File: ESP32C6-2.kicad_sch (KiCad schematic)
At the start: 20 parts, among them J1 DE9_Pins, J2 Screw_Terminal_01x04, U1 XIAO-ESP32-C6/SUPERMini, U2 SN65HVD230DR, U3 LMR51430YDDCR

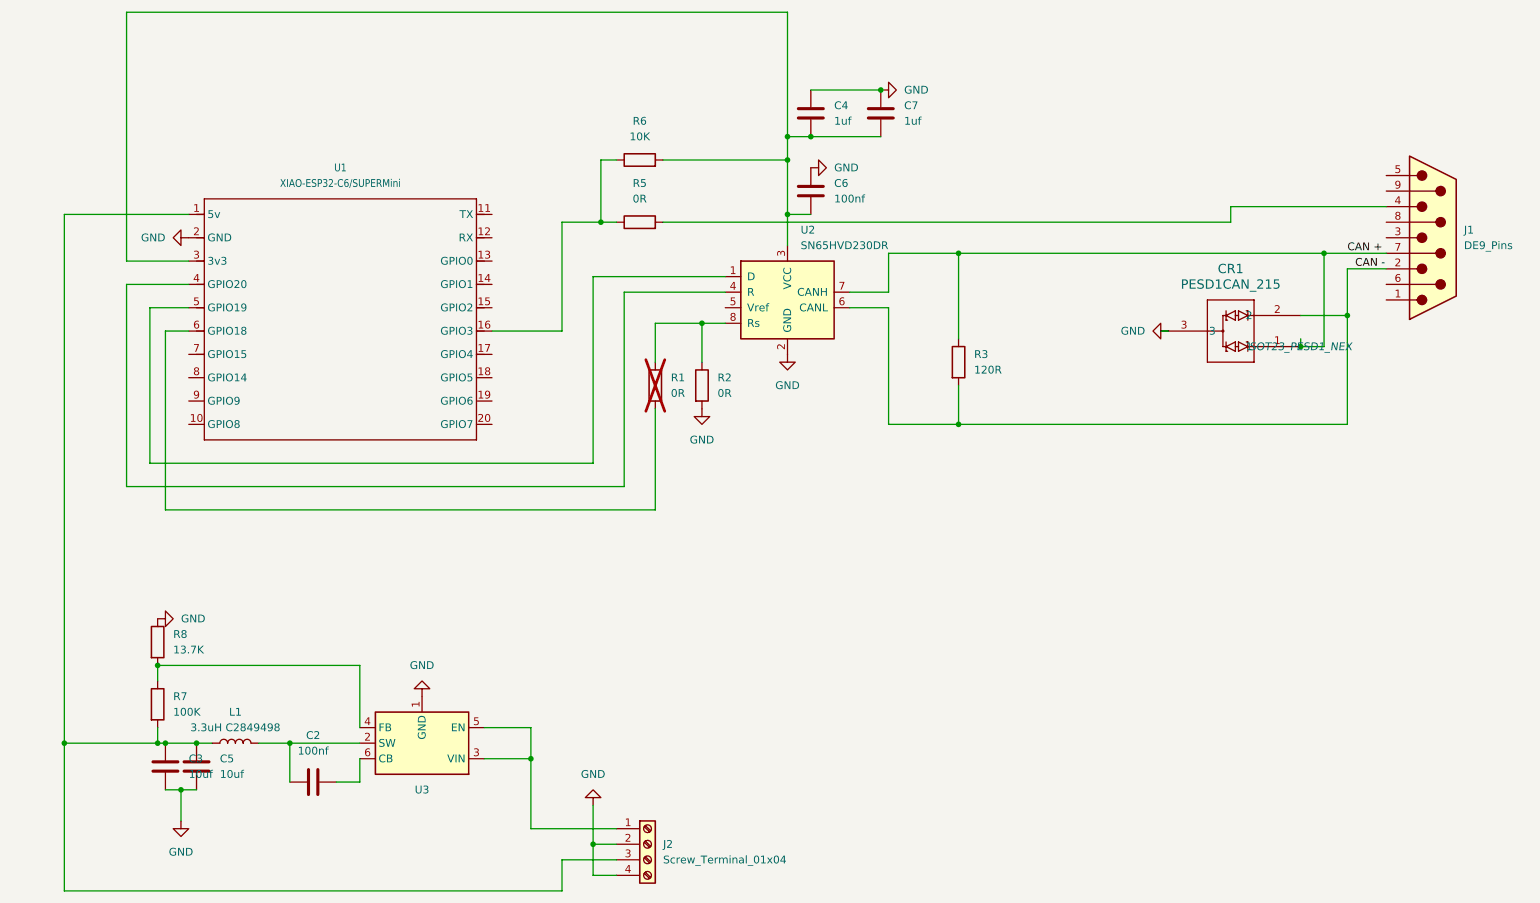
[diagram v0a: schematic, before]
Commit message: Update to add TVS and ground plane
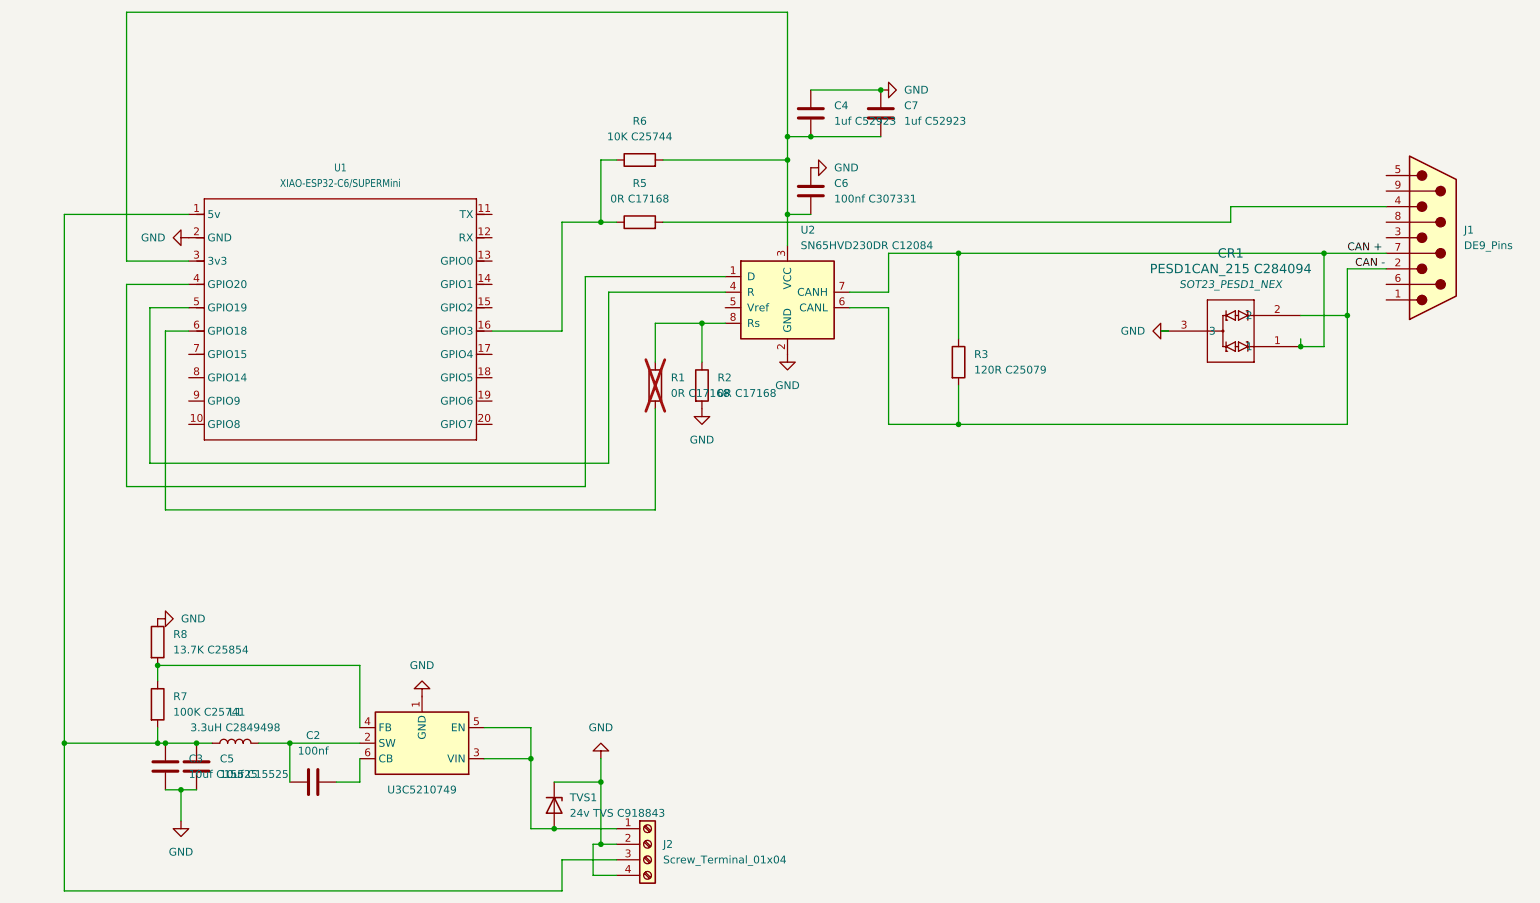
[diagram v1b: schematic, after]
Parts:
- added TVS1: 24v TVS C918843, JPGIndustriesCustom:TVS SOD-123FL_L3.0-W1.8-LS3.7-RD C918843, symbol Diode:PTVS5V0Z1USK
- C3, C5: value 10uf -> 10uf C15525
- C4, C7: value 1uf -> 1uf C52923
- C6: value 100nf -> 100nf C307331
- CR1: value PESD1CAN_215 -> PESD1CAN_215 C284094
- J1, J2: now left out of the parts list
- R1: value 0R -> 0R C17168; now left out of the parts list
- R2, R5: value 0R -> 0R C17168
- R3: value 120R -> 120R C25079
- R6: value 10K -> 10K C25744
- R7: value 100K -> 100K C25741
- R8: value 13.7K -> 13.7K C25854
- U2: value SN65HVD230DR -> SN65HVD230DR C12084
- renumbered U3 to U3C5210749
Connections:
- net GND: now also TVS1.1 (K)
- net at U1.4 (GPIO20): now also U2.1 (D); no longer U2.4 (R)
- net at U1.5 (GPIO19): now also U2.4 (R); no longer U2.1 (D)
- net at J2.1 (Pin_1), U3C5210749.3 (VIN), U3C5210749.5 (EN): now also TVS1.2 (A)

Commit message: Rev 1, as built
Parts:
- added C1, C8: 4.7uf, Capacitor_SMD:C_0402_1005Metric_Pad0.74x0.62mm_HandSolder, symbol Device:C
- C2: value 100nf -> 100nf C307331
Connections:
- net GND: now also TVS1.2 (A), C1.1, C8.1; no longer TVS1.1 (K)
- net +5V: now reaches C3.1, C5.1, J2.3 (Pin_3), L1.1, R7.2, U1.1 (5v)
- net at J2.1 (Pin_1), U3C5210749.3 (VIN), U3C5210749.5 (EN): now also TVS1.1 (K), C1.2, C8.2; no longer TVS1.2 (A)
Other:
- moved on the sheet: TVS1
